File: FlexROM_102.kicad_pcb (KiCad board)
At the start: 2 copper layers, 35.6 x 17.8 mm, 6 parts, among them J1 27C256 DIP LEGS, U1 28C256

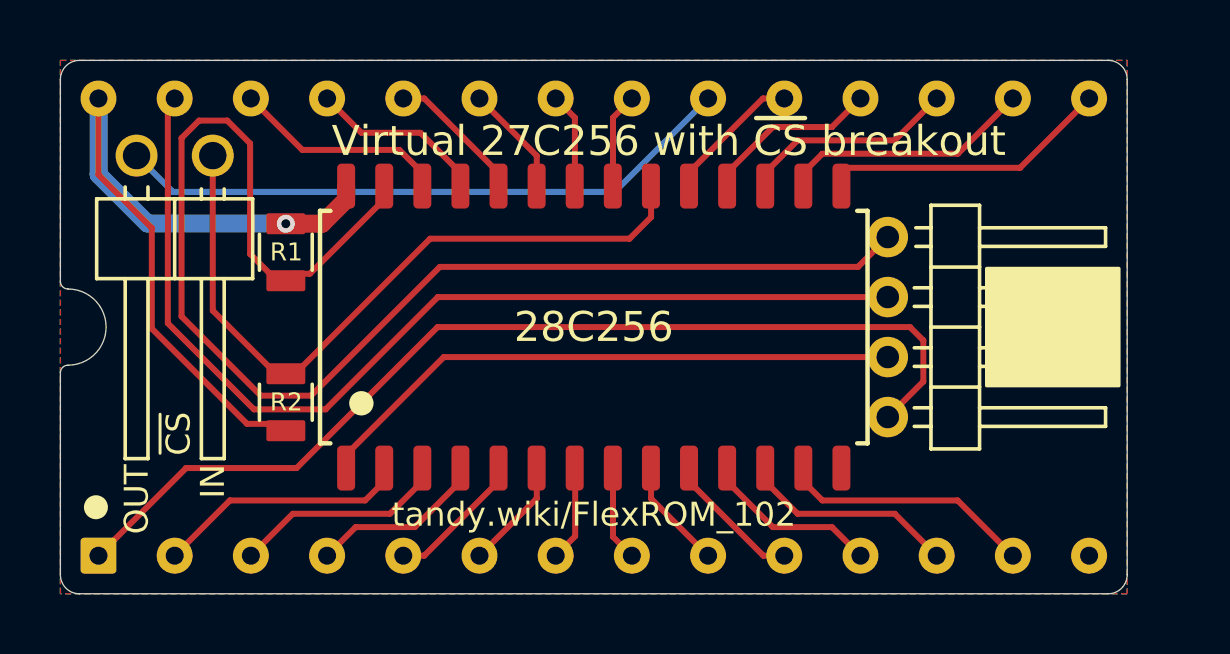
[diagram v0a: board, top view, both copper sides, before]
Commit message: flexrom 102 & 200 accept eeprom or fram
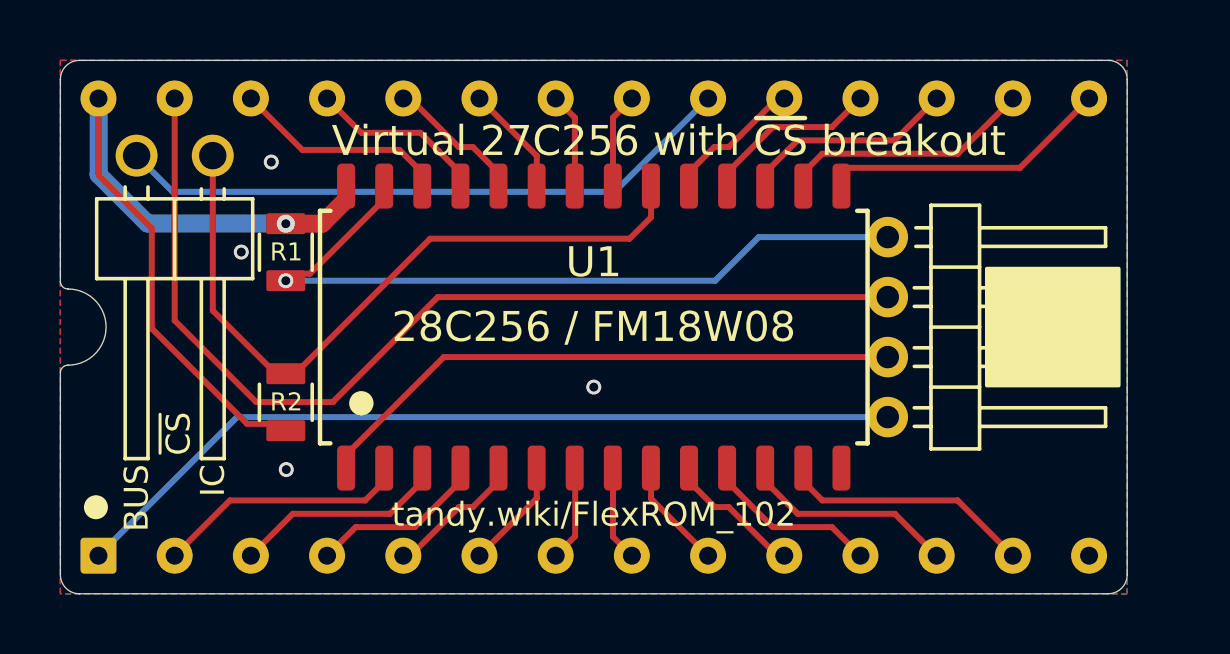
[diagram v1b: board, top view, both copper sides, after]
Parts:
- U1: value 28C256 -> 28C256 / FM18W08
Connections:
- net /~{CS_OUT} renamed /~{CS}_BUS
- JP1 pad 1: /~{CS_IN} -> /~{CS}_IC
- R2 pad 1: /~{CS_IN} -> /~{CS}_IC
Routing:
- net /~{CS}_IC: track 0.00 -> 23.8 mm
- net /~{CS_IN}: track 23.8 -> 0.00 mm
- net /~{WE}: track 45.7 -> 25.5 mm, vias 0 -> 1
- net /NC_A14: track 33.9 -> 28.2 mm
- net /A14_~{WE}: track 34.3 -> 33.8 mm
- net GND: vias 0 -> 4
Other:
- board text added: "BUS"
- board text added: "IC"
- board text added: "R1,R2: ${00000000-0000-0000-0000-00005f9fca43:VALUE} Legs: TE 1544210 or Mill-Max 3121"
- board text added: "To boot from EEPROM/FRAM: Connect ~{CS}_BUS to ~{CS}_IC To boot from REX_Classic: Connect ~{CS}_BUS to REX TP1"
- board text removed: "Boot from internal main rom: Connect ~{CS}_OUT to ~{CS}_IN Boot from REX_Classic main rom: Connect ~{CS}_OUT to REX TP1"
- board text removed: "IN"
- board text removed: "OUT"
- board text removed: "R1,R2: ${00000000-0000-0000-0000-00005f9fca43:VALUE} Legs: TE 1544210"

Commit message: minor touches
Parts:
- added C1: 0.1uF, 000_LOCAL:C_0805, F.Cu at (116.7, 97.5)
- R1, R2: value 47K -> 100K
- moved R1 2.50 mm to (116.7, 101.6)
- moved R2 1.60 mm to (116.7, 105.7)
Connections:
- U1 pad 20: /~{CS_IN} -> /~{CS}_IC
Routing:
- net VCC: track 26.5 -> 30.8 mm
- net /~{WE}: track 25.5 -> 29.4 mm
- net /~{CS}_IC: track 23.8 -> 26.8 mm
- net /A14_~{WE}: track 33.8 -> 36.4 mm
- net GND: vias 4 -> 16
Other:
- board text added: "C1: ${a3f6ca9c-7216-486f-a501-174707a1552f:VALUE} R1,R2: ${00000000-0000-0000-0000-00005f9fca43:VALUE} Legs: TE 1544210 or Mill-Max 3121"
- board text removed: "R1,R2: ${00000000-0000-0000-0000-00005f9fca43:VALUE} Legs: TE 1544210 or Mill-Max 3121"

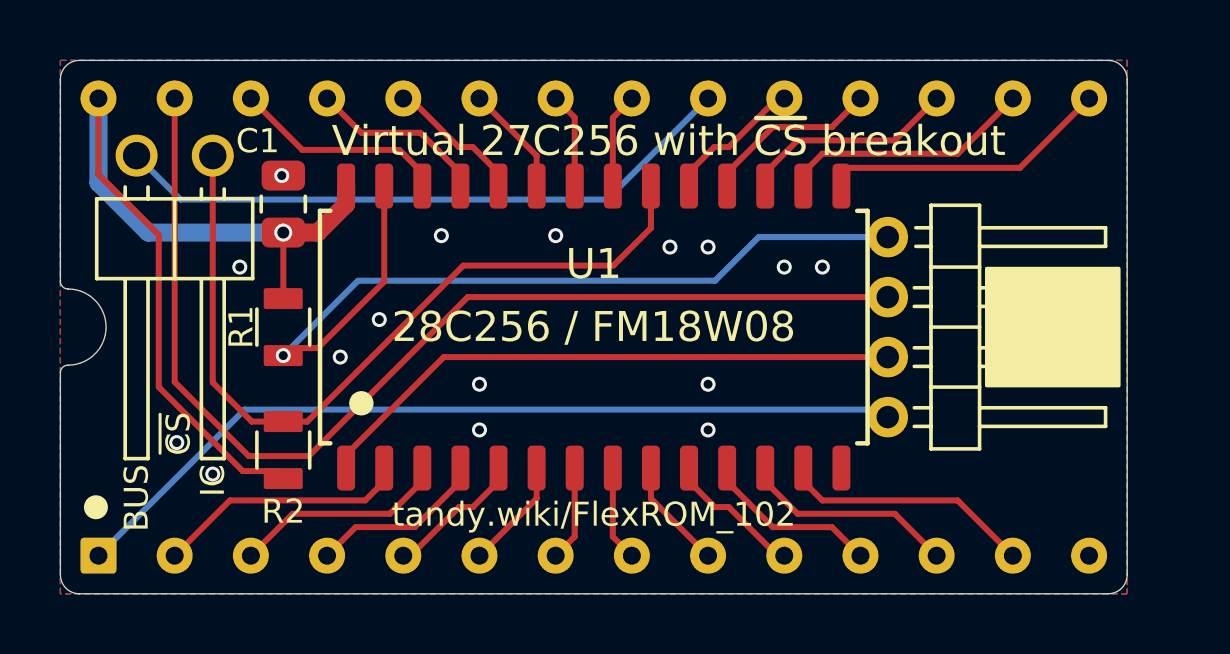
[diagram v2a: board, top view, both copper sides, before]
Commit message: add SM8 DIP8, readme
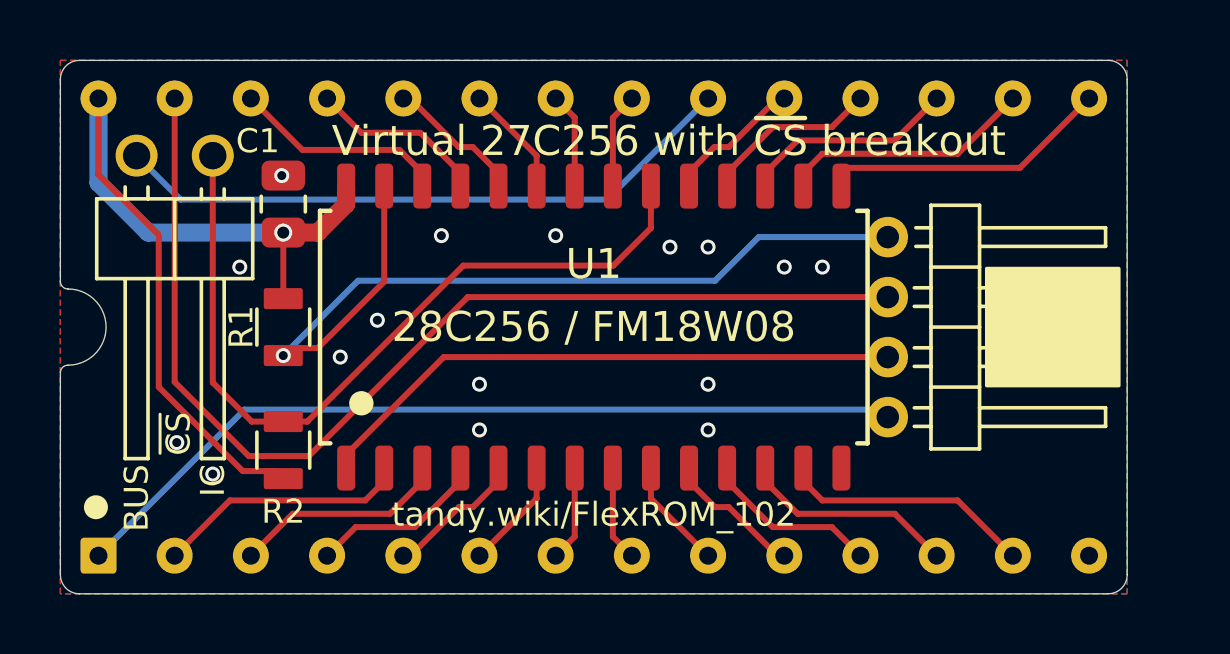
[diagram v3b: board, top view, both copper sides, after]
